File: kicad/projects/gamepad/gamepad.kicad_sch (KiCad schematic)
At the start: 49 parts, among them J1 peripheral_addr_bus_connector, J2 peripheral_aux_connector, J3 peripheral_membank_connector, J4 Conn_01x02_Socket, J5 Conn_01x02_Socket, J6 Conn_02x05_Odd_Even, U1 74HC161, U10 74HC245, U11 74HC245, U12 74HC245, U13 74HC245, U2 74HC161, U3 74HC595, U4 74HC595, U5 74HC595, U6 74HC595, U7 74HC14, U8 74HC08, U9 74HC109

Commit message: Start work on gamepad schematic.
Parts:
- added C10, C11, C12, C13: C, Capacitor_THT:C_Disc_D5.0mm_W2.5mm_P5.00mm, symbol Device:C
- added J7, J8: Conn_01x05_Socket, symbol Connector:Conn_01x05_Socket
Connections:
- net DATA_BUS_00: now also U13.9 (A8)
- net DATA_BUS_01: now also U13.8 (A7)
- net DATA_BUS_02: now also U13.7 (A6)
- net DATA_BUS_03: now also U13.6 (A5)
- net DATA_BUS_04: now also U13.5 (A3)
- net DATA_BUS_05: now also U13.4 (A3)
- net DATA_BUS_06: now also U13.3 (A2)
- net DATA_BUS_07: now also U13.2 (A1)
- net DATA_BUS_08: now also U12.9 (A8)
- net DATA_BUS_09: now also U12.8 (A7)
- net DATA_BUS_10: now also U12.7 (A6)
- net DATA_BUS_11: now also U12.6 (A5)
- net DATA_BUS_12: now also U12.5 (A3)
- net DATA_BUS_13: now also U12.4 (A3)
- net DATA_BUS_14: now also U12.3 (A2)
- net DATA_BUS_15: now also U12.2 (A1)
- net GND: now also C1.2, C2.2, C3.2, C4.2, U1.8 (GND), U12.1 (DIR), U12.10 (GND), U13.1 (DIR), U13.10 (GND), U2.3 (P0), U2.4 (P1), U2.5 (P2), U2.6 (P3), U2.8 (GND), U3.13 (~{OE}), U3.8 (GND), U4.13 (~{OE}), U4.8 (GND), U9.3 (~{K}), C12.2, C13.2
- net VCC: now also C1.1, C2.1, C3.1, C4.1, U1.1 (~{MR}), U1.10 (TE), U1.16 (VCC), U1.7 (PE), U1.9 (~{SPE}), U12.20 (VCC), U13.20 (VCC), U2.1 (~{MR}), U2.10 (TE), U2.16 (VCC), U2.7 (PE), U2.9 (~{SPE}), U3.10 (~{SRCLR}), U3.16 (VCC), U4.10 (~{SRCLR}), U4.16 (VCC), U9.1 (~{CLR}), U9.2 (J), U9.5 (~{PRE}), C12.1, C13.1
- net PAD 1 LED 7: now reaches D8.2 (A)
- net PAD 1 LED 7: now also U10.12 (B7)
- net at U2.15 (TC): now also U8.1
- net SHIFT SERIAL CLK: now reaches U2.2 (CP)
- net SHIFT SERIAL CLK: now also U9.6 (Q)
- net at U11.1 (DIR): now also U11.20 (VCC)
- net PAD 1 ADDR LED: now reaches U11.11 (B8)
- net PAD 1 ADDR LED: now also D13.1 (K)
- net PAD 2 ADDR LED: now reaches U11.12 (B7)
- net PAD 2 ADDR LED: now also D14.1 (K)
- net PAD 1 LED 0: now reaches U11.13 (B6)
- net PAD 1 LED 0: now also D1.2 (A)
- net PAD 1 LED 1: now reaches U11.14 (B5)
- net PAD 1 LED 1: now also D2.2 (A)
- net PAD 1 LED 2: now reaches U11.15 (B4)
- net PAD 1 LED 2: now also D3.2 (A)
- net PAD 1 LED 3: now reaches U11.16 (B3)
- net PAD 1 LED 3: now also D4.2 (A)
- net PAD 1 LED 4: now reaches U11.17 (B2)
- net PAD 1 LED 4: now also D5.2 (A)
- net PAD 1 LED 5: now reaches U11.18 (B1)
- net PAD 1 LED 5: now also D6.2 (A)
- net PAD 1 SHIFT 07: now reaches U11.2 (A1)
- net PAD 1 SHIFT 07: now also U13.18 (B1), U4.15 (QA)
- net PAD 1 SHIFT 06: now reaches U11.3 (A2)
- net PAD 1 SHIFT 06: now also U13.17 (B2), U4.1 (QB)
- net PAD 1 SHIFT 05: now reaches U11.4 (A3)
- net PAD 1 SHIFT 05: now also U13.16 (B3), U4.2 (QC)
- net PAD 1 SHIFT 04: now reaches U11.5 (A3)
- net PAD 1 SHIFT 04: now also U13.15 (B4), U4.3 (QD)
- net PAD 1 SHIFT 03: now reaches U11.6 (A5)
- net PAD 1 SHIFT 03: now also U13.14 (B5), U4.4 (QE)
- net PAD 1 SHIFT 02: now reaches U11.7 (A6)
- net PAD 1 SHIFT 02: now also U13.13 (B6), U4.5 (QF)
- net PAD 1 SHIFT 01: now reaches U11.8 (A7)
- net PAD 1 SHIFT 01: now also U13.12 (B7), U4.6 (QG)
- net PAD 1 SHIFT 00: now reaches U11.9 (A8)
- net PAD 1 SHIFT 00: now also U13.11 (B8), U4.7 (QH)
- net PAD 1 LED 6: now reaches D7.2 (A)
- net PAD 1 LED 6: now also U10.11 (B8)
- net at U8.10: now also U8.3, U8.5
- net SHIFT OUT REG CLK: now reaches U8.8
- net SHIFT OUT REG CLK: now also C11.1
- net BASE CLK: now reaches U8.9
- net BASE CLK: now also J6.10 (Pin_10), J6.2 (Pin_2), J6.4 (Pin_4), J6.6 (Pin_6), J6.8 (Pin_8), U7.1, U9.4 (C)
- net at J6.1 (Pin_1): now also U1.2 (CP)
- net CLK DIV 2: now reaches J6.3 (Pin_3)
- net CLK DIV 2: now also U1.14 (Q0)
- net CLK DIV 4: now reaches J6.5 (Pin_5)
- net CLK DIV 4: now also U1.13 (Q1)
- net CLK DIV 8: now reaches J6.7 (Pin_7)
- net CLK DIV 8: now also U1.12 (Q2)
- net CLK DIV 16: now reaches J6.9 (Pin_9)
- net CLK DIV 16: now also U1.11 (Q3)
- net PAD 1 LED 11: now reaches D12.2 (A)
- net PAD 1 LED 11: now also U10.16 (B3)
- net at U10.1 (DIR): now also U10.20 (VCC)
- net PAD 1 LED 8: now reaches U10.13 (B6)
- net PAD 1 LED 8: now also D9.2 (A)
- net PAD 1 LED 9: now reaches U10.14 (B5)
- net PAD 1 LED 9: now also D10.2 (A)
- net PAD 1 LED 10: now reaches U10.15 (B4)
- net PAD 1 LED 10: now also D11.2 (A)
- net PAD 1 SHIFT 15: now reaches U10.2 (A1)
- net PAD 1 SHIFT 15: now also U12.18 (B1), U3.15 (QA)
- net PAD 1 SHIFT 14: now reaches U10.3 (A2)
- net PAD 1 SHIFT 14: now also U12.17 (B2), U3.1 (QB)
- net PAD 1 SHIFT 13: now reaches U10.4 (A3)
- net PAD 1 SHIFT 13: now also U12.16 (B3), U3.2 (QC)
- net PAD 1 SHIFT 12: now reaches U10.5 (A3)
- net PAD 1 SHIFT 12: now also U12.15 (B4), U3.3 (QD)
- net PAD 1 SHIFT 11: now reaches U10.6 (A5)
- net PAD 1 SHIFT 11: now also U12.14 (B5), U3.4 (QE)
- net PAD 1 SHIFT 10: now reaches U10.7 (A6)
- net PAD 1 SHIFT 10: now also U12.13 (B6), U3.5 (QF)
- net PAD 1 SHIFT 09: now reaches U10.8 (A7)
- net PAD 1 SHIFT 09: now also U12.12 (B7), U3.6 (QG)
- net PAD 1 SHIFT 08: now reaches U10.9 (A8)
- net PAD 1 SHIFT 08: now also U12.11 (B8), U3.7 (QH)
- net at U7.4: now also U3.14 (SER)
- net ~{BASE CLK}: now reaches U8.4
- net ~{BASE CLK}: now also U7.2
- net GAMEPAD LATCH: now reaches U8.6
- net GAMEPAD LATCH: now also C10.1
- net GAMEPAD CLK: now reaches U9.7 (~{Q})
- net GAMEPAD CLK: now also U8.2
- net ~{PAD 1 OE}: now reaches U13.19 (~{OE})
- net ~{PAD 1 OE}: now also U12.19 (~{OE})
- net at U4.11 (SRCLK): now also U3.11 (SRCLK)
- net at U4.12 (RCLK): now also U3.12 (RCLK)
- net at U4.14 (SER): now also U3.9 (QH')
- no-connect marks 0 -> 8
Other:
- moved on the sheet: C1, C2, C3, C4, D1, D10, D11, D12, D13, D14, D2, D3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

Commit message: Gamepad schematic done.
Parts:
- added C14: C, Capacitor_THT:C_Disc_D5.0mm_W2.5mm_P5.00mm, symbol Device:C
- added J10: Pad 2 SNES, Connector_PinSocket_2.54mm:PinSocket_1x05_P2.54mm_Horizontal, symbol Connector:Conn_01x05_Socket
- added J11: Conn_01x03_Pin, Connector_PinHeader_2.54mm:PinHeader_1x03_P2.54mm_Horizontal, symbol Connector:Conn_01x03_Pin
- added J9: Pad 2 header, Connector_PinSocket_2.54mm:PinSocket_1x05_P2.54mm_Horizontal, symbol Connector:Conn_01x05_Socket
- added R3: 10K, Resistor_THT:R_Axial_DIN0207_L6.3mm_D2.5mm_P10.16mm_Horizontal, symbol Device:R_US
- added TP1: Gamepad Latch, Connector_Pin:Pin_D1.0mm_L10.0mm, symbol Connector:TestPoint
- added TP2: Shift out reg CLK, Connector_Pin:Pin_D1.0mm_L10.0mm, symbol Connector:TestPoint
- added TP3: Shift Serial CLK, Connector_Pin:Pin_D1.0mm_L10.0mm, symbol Connector:TestPoint
- added TP4: Gamepad CLK, Connector_Pin:Pin_D1.0mm_L10.0mm, symbol Connector:TestPoint
- added TP5: Base CLK, Connector_Pin:Pin_D1.0mm_L10.0mm, symbol Connector:TestPoint
- added TP6: ~{Base CLK}, Connector_Pin:Pin_D1.0mm_L10.0mm, symbol Connector:TestPoint
- added TP7: RCO, Connector_Pin:Pin_D1.0mm_L10.0mm, symbol Connector:TestPoint
- added U14: 74HC00, Package_DIP:DIP-14_W7.62mm_Socket, symbol 74xx:74HC00
- J4: value Conn_01x02_Socket -> PAD 1 ACTIVE
- J5: value Conn_01x02_Socket -> PAD 2 ACTIVE
- J7: value Conn_01x05_Socket -> Pad 1 header; footprint (none) -> Connector_PinSocket_2.54mm:PinSocket_1x05_P2.54mm_Horizontal
- J8: value Conn_01x05_Socket -> Pad 1 SNES; footprint (none) -> Connector_PinSocket_2.54mm:PinSocket_1x05_P2.54mm_Horizontal
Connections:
- net BASE CLK: now also TP5.1
- net CTL_CLK: now also J6.1 (Pin_1), U1.2 (CP)
- net DATA_BUS_00: now also U6.7 (QH)
- net DATA_BUS_01: now also U6.6 (QG)
- net DATA_BUS_02: now also U6.5 (QF)
- net DATA_BUS_03: now also U6.4 (QE)
- net DATA_BUS_04: now also U6.3 (QD)
- net DATA_BUS_05: now also U6.2 (QC)
- net DATA_BUS_06: now also U6.1 (QB)
- net DATA_BUS_07: now also U6.15 (QA)
- net DATA_BUS_08: now also U5.7 (QH)
- net DATA_BUS_09: now also U5.6 (QG)
- net DATA_BUS_10: now also U5.5 (QF)
- net DATA_BUS_11: now also U5.4 (QE)
- net DATA_BUS_12: now also U5.3 (QD)
- net DATA_BUS_13: now also U5.2 (QC)
- net DATA_BUS_14: now also U5.1 (QB)
- net DATA_BUS_15: now also U5.15 (QA)
- net GAMEPAD CLK: now also J7.4 (Pin_4), J8.4 (Pin_4), J10.4 (Pin_4), J9.4 (Pin_4), TP4.1
- net GAMEPAD LATCH: now also J7.3 (Pin_3), J8.3 (Pin_3), J10.3 (Pin_3), J9.3 (Pin_3), TP1.1
- net GND: now also C10.2, C11.2, C5.2, C6.2, C7.2, C8.2, C9.2, J7.1 (Pin_1), J8.1 (Pin_1), RN1.1 (common), RN2.1 (common), U10.10 (GND), U11.10 (GND), U5.8 (GND), U6.8 (GND), U7.11, U7.13, U7.7 (GND), U7.9, U8.12, U8.13, U8.7 (GND), U9.12 (C), U9.13 (~{K}), U9.14 (J), U9.8 (GND), C14.2, J10.1 (Pin_1), J11.3 (Pin_3), J9.1 (Pin_1), R3.2, U14.10, U14.12, U14.13, U14.7 (GND), U14.9
- net RFM: now also U14.2, U14.4
- net SHIFT OUT REG CLK: now also U3.12 (RCLK), U4.12 (RCLK), U5.12 (RCLK), U6.12 (RCLK), TP2.1
- net SHIFT SERIAL CLK: now also U3.11 (SRCLK), U4.11 (SRCLK), U5.11 (SRCLK), U6.11 (SRCLK), TP3.1
- net VCC: now also C5.1, C6.1, C7.1, C8.1, C9.1, J7.5 (Pin_5), J8.5 (Pin_5), R1.2, R2.2, U10.1 (DIR), U10.20 (VCC), U11.1 (DIR), U11.20 (VCC), U5.10 (~{SRCLR}), U5.16 (VCC), U6.10 (~{SRCLR}), U6.16 (VCC), U7.14 (VCC), U8.14 (VCC), U9.11 (~{PRE}), U9.15 (~{CLR}), U9.16 (VCC), C14.1, J10.5 (Pin_5), J11.1 (Pin_1), J9.5 (Pin_5), U14.14 (VCC)
- net ~{BASE CLK}: now also TP6.1
- net at D8.1 (K): now also RN1.3 (R2)
- net PAD 2 DATA: now reaches U7.5
- net PAD 2 DATA: now also J10.2 (Pin_2), J9.2 (Pin_2)
- net at U7.6: now also U5.14 (SER)
- net PAD 2 ACTIVE: now reaches J5.1 (Pin_1)
- net PAD 2 ACTIVE: now also J5.2 (Pin_2), U14.1
- net at U2.15 (TC), U8.1: now also TP7.1
- net ~{LED ENABLE}: now reaches U11.19 (~{OE})
- net ~{LED ENABLE}: now also U10.19 (~{OE}), J11.2 (Pin_2), R3.1
- net at D6.1 (K): now also RN2.7 (R6)
- net at D7.1 (K): now also RN1.2 (R1)
- net at D2.1 (K): now also RN2.3 (R2)
- net at D1.1 (K): now also RN2.2 (R1)
- net at D12.1 (K): now also RN1.7 (R6)
- net at D3.1 (K): now also RN2.4 (R3)
- net PAD 1 DATA: now reaches U7.3
- net PAD 1 DATA: now also J7.2 (Pin_2), J8.2 (Pin_2)
- net PAD 1 ACTIVE: now reaches J4.1 (Pin_1)
- net PAD 1 ACTIVE: now also J4.2 (Pin_2), U14.5
- net at D11.1 (K): now also RN1.6 (R5)
- net at R2.1: now also D14.2 (A)
- net at D13.2 (A): now also R1.1
- net PAD 2 ~{OE}: now reaches U5.13 (~{OE})
- net PAD 2 ~{OE}: now also U6.13 (~{OE}), U14.3
- net at U5.9 (QH'): now also U6.14 (SER)
- net at D5.1 (K): now also RN2.6 (R5)
- net at D9.1 (K): now also RN1.4 (R3)
- net at D10.1 (K): now also RN1.5 (R4)
- net at RN2.5 (R4): now also D4.1 (K)
- net ADDR_BUS_00: no longer names the net of J1.17 (A_00)
- net ADDR_BUS_01: no longer names the net of J1.18 (A_01)
- net ADDR_BUS_02: no longer names the net of J1.19 (A_02)
- net ADDR_BUS_03: no longer names the net of J1.20 (A_03)
- net ADDR_BUS_04: no longer names the net of J1.21 (A_04)
- net ADDR_BUS_05: no longer names the net of J1.22 (A_05)
- net ADDR_BUS_06: no longer names the net of J1.23 (A_06)
- net ADDR_BUS_07: no longer names the net of J1.24 (A_07)
- net ADDR_BUS_08: no longer names the net of J1.25 (A_08)
- net ADDR_BUS_09: no longer names the net of J1.26 (A_09)
- net ADDR_BUS_10: no longer names the net of J1.27 (A_10)
- net ADDR_BUS_11: no longer names the net of J1.28 (A_11)
- net ADDR_BUS_12: no longer names the net of J1.29 (A_12)
- net ADDR_BUS_13: no longer names the net of J1.30 (A_13)
- net ADDR_BUS_14: no longer names the net of J1.31 (A_14)
- net ADDR_BUS_15: no longer names the net of J1.32 (A_15)
- net BANK_BUS_00: no longer names the net of J3.1 (B_00)
- net BANK_BUS_01: no longer names the net of J3.2 (B_01)
- net BANK_BUS_02: no longer names the net of J3.3 (B_02)
- net BANK_BUS_03: no longer names the net of J3.4 (B_03)
- net BANK_BUS_04: no longer names the net of J3.5 (B_04)
- net BANK_BUS_05: no longer names the net of J3.6 (B_05)
- net BANK_BUS_06: no longer names the net of J3.7 (B_06)
- net BANK_BUS_07: no longer names the net of J3.8 (B_07)
- net BANK_BUS_08: no longer names the net of J3.9 (B_08)
- net BANK_BUS_09: no longer names the net of J3.10 (B_09)
- net BANK_BUS_10: no longer names the net of J3.11 (B_10)
- net BANK_BUS_11: no longer names the net of J3.12 (B_11)
- net BANK_BUS_12: no longer names the net of J3.13 (B_12)
- net BANK_BUS_13: no longer names the net of J3.14 (B_13)
- net BANK_BUS_14: no longer names the net of J3.15 (B_14)
- net BANK_BUS_15: no longer names the net of J3.16 (B_15)
- net ~{PAD 1 OE} renamed PAD 1 ~{OE}
- net PAD 1 ~{OE}: now also U14.6
- no-connect marks 8 -> 56
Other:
- note added: "Clock divide by 2"
- note added: "Count to 16"
- note added: "Gamepad 1 bus output"
- note added: "Gamepad 1 shifter"
- note added: "Gamepad 1 status and pads addressed LEDs"
- note added: "Gamepad 2 shifter"
- note added: "Gamepad connections"
- note added: "LED enable"
- note added: "Latch and clock timing"
- note added: "Optional input clock divide"
- moved on the sheet: C1, C10, C11, C12, C13, C2, C3, C4, C5, C6, C7, C8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

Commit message: Start routing gamepad PCB.
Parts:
- removed U8: 74HC08, Package_DIP:DIP-14_W7.62mm_Socket, symbol sixteen-bit-computer:74HC08
- removed U9: 74HC109, Package_DIP:DIP-16_W7.62mm_Socket, symbol sixteen-bit-computer:74HC109
- added R4: 10K, Resistor_THT:R_Axial_DIN0207_L6.3mm_D2.5mm_P10.16mm_Horizontal, symbol Device:R_US
- added TP8: Raw Gamepad Latch, Connector_Pin:Pin_D1.0mm_L10.0mm, symbol Connector:TestPoint
- added TP9: Raw Shift out reg CLK, Connector_Pin:Pin_D1.0mm_L10.0mm, symbol Connector:TestPoint
- added U8: 74HC00, Package_DIP:DIP-14_W7.62mm_Socket, symbol 74xx:74HC00
- added U9: 74HC161, Package_DIP:DIP-16_W7.62mm_Socket, symbol sixteen-bit-computer:74HC161
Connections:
- net BASE CLK: now also U14.12, R4.2, U9.2 (CP)
- net GAMEPAD CLK: now also U14.5, U7.8
- net GAMEPAD LATCH: now also U7.12; no longer C10.1
- net GND: now also R4.1, U8.10, U8.12, U8.13, U8.7 (GND), U8.9, U9.3 (P0), U9.4 (P1), U9.5 (P2), U9.6 (P3), U9.8 (GND); no longer U14.10, U14.12, U14.13, U14.9, U7.11, U7.13, U7.9
- net PAD 1 ACTIVE: now also U8.5; no longer U14.5
- net PAD 1 ~{OE}: now also U8.6; no longer U14.6
- net PAD 2 ACTIVE: now also U8.1; no longer U14.1
- net PAD 2 ~{OE}: now also U8.3; no longer U14.3
- net RFM: now also U8.2, U8.4; no longer U14.2, U14.4
- net SHIFT OUT REG CLK: now also U7.10; no longer C11.1
- net SHIFT SERIAL CLK: now also U7.9, U9.14 (Q0)
- net VCC: now also U8.14 (VCC), U9.1 (~{MR}), U9.10 (TE), U9.16 (VCC), U9.7 (PE), U9.9 (~{SPE})
- net ~{BASE CLK}: now also U14.9
- net at TP7.1, U2.15 (TC): now also U14.4
- net at U14.11: now also C11.1, U7.11, TP9.1
- net at U14.8: now also C10.1, U7.13, TP8.1
- new net: U14.1, U14.2, U14.6
- new net: U14.10, U14.13, U14.3
- no-connect marks 56 -> 54
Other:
- note added: "Clock div by 2"
- note removed: "Clock divide by 2"
- moved on the sheet: C1, C10, C11, C12, C13, C14, C2, C3, C4, C5, C6, C7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

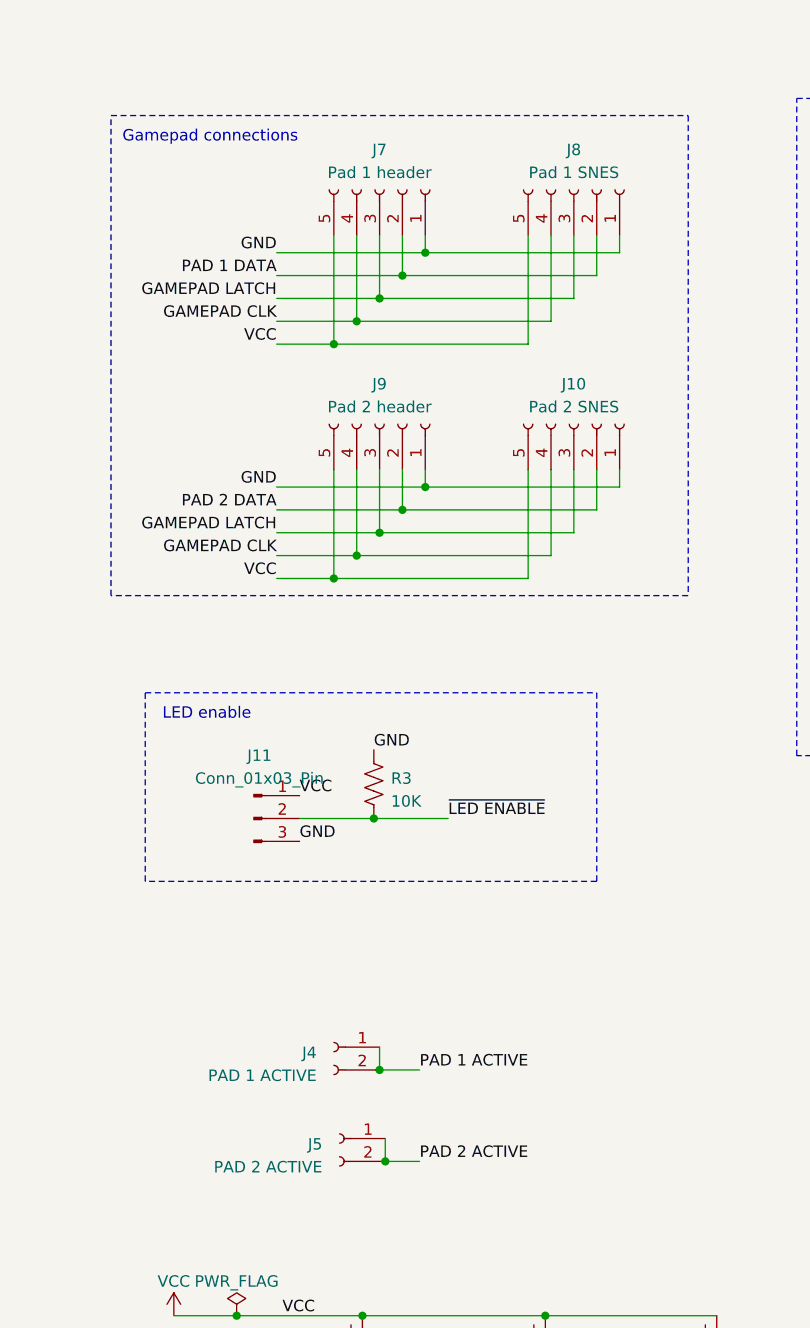
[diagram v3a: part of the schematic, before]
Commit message: Add gamepad connector and almost complete on gamepad PCB
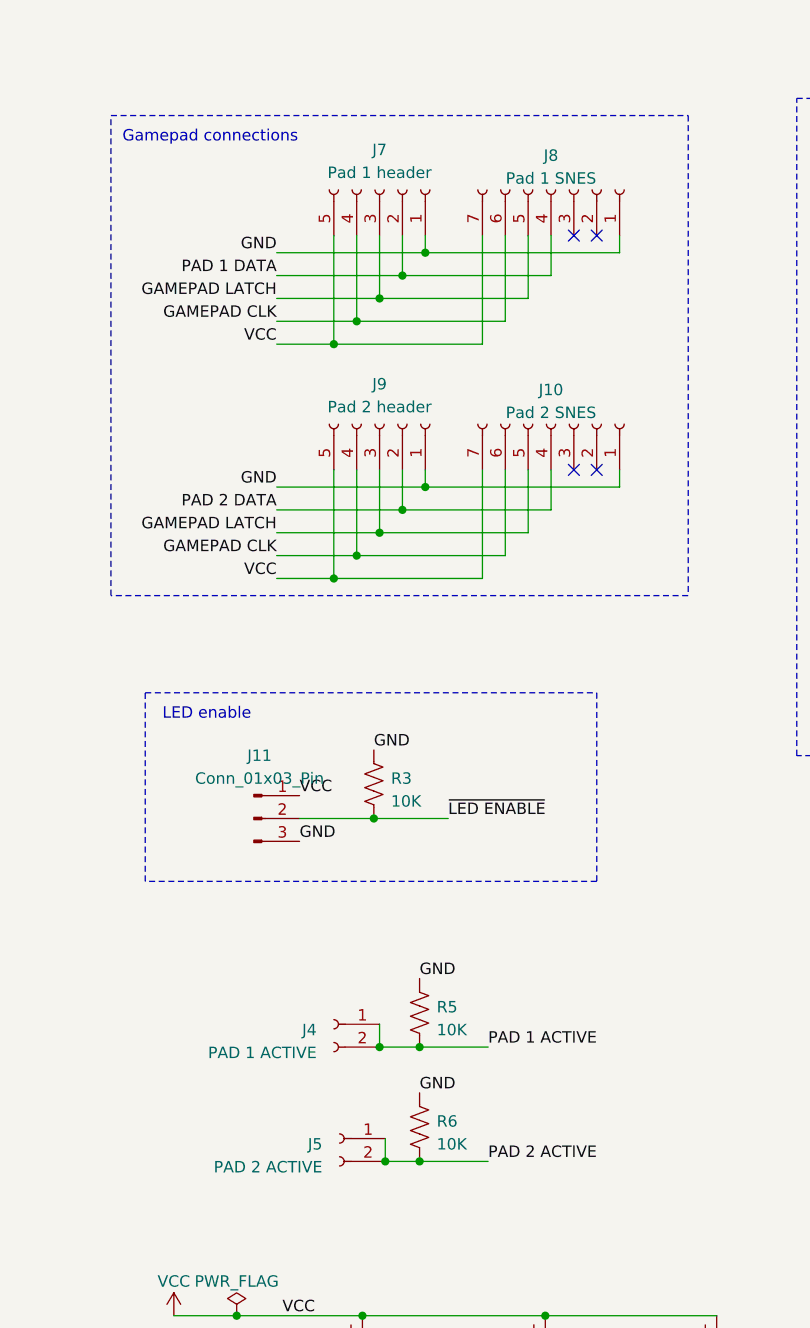
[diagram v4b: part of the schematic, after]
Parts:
- removed J10: Pad 2 SNES, Connector_PinSocket_2.54mm:PinSocket_1x05_P2.54mm_Horizontal, symbol Connector:Conn_01x05_Socket
- removed J8: Pad 1 SNES, Connector_PinSocket_2.54mm:PinSocket_1x05_P2.54mm_Horizontal, symbol Connector:Conn_01x05_Socket
- added J10: Pad 2 SNES, sixteen-bit-computer:snes-rightangle-connector, symbol Connector:Conn_01x07_Socket
- added J8: Pad 1 SNES, sixteen-bit-computer:snes-rightangle-connector, symbol Connector:Conn_01x07_Socket
- added R5, R6: 10K, Resistor_THT:R_Axial_DIN0207_L6.3mm_D2.5mm_P10.16mm_Horizontal, symbol Device:R_US
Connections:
- net GAMEPAD CLK: now also J10.6 (Pin_6), J8.6 (Pin_6)
- net GAMEPAD LATCH: now also J10.5 (Pin_5), J8.5 (Pin_5)
- net GND: now also J10.1 (Pin_1), J8.1 (Pin_1), R5.2, R6.2
- net PAD 1 ACTIVE: now also R5.1
- net PAD 1 DATA: now also J8.4 (Pin_4)
- net PAD 2 ACTIVE: now also R6.1
- net PAD 2 DATA: now also J10.4 (Pin_4)
- net VCC: now also J10.7 (Pin_7), J8.7 (Pin_7)
- no-connect marks 54 -> 58
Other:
- moved on the sheet: J4

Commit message: Gamepad updated to single wie rfm wtm.
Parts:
- added C15, C16: C, Capacitor_THT:C_Disc_D5.0mm_W2.5mm_P5.00mm, symbol Device:C
- C97, C98, C99: value C_Polarized -> 33uF
- R1, R2: value R_US -> 1K
- RN1, RN2: value R_Network08_US -> 2K
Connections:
- net GND: now also C15.1, C16.1; no longer U8.10, U8.12, U8.13, U8.9
- net VCC: now also C15.2, C16.2
- net MEMACTIVE_RFM: now reaches U8.11
- net MEMACTIVE_RFM: now also U8.2, U8.4
- net at U8.8: now also U8.12
- removed net RFM: J2.10 (RFM), U8.2, U8.4
- net WTM renamed RFM_WTM
- net RFM_WTM: now also U8.10, U8.9
- new net MEM_ACTIVE: J2.10 (MEM_ACT), U8.13
- no-connect marks 58 -> 56
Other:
- moved on the sheet: J2, U8D

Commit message: Gamepad updates. Fix memactive RFM. Fix miswired Pad 1 data and pas 1 and 2 read LEDs.
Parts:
- added C17: C, Capacitor_THT:C_Disc_D5.0mm_W2.5mm_P5.00mm, symbol Device:C
- added U15: 74HC00, Package_DIP:DIP-14_W7.62mm_Socket, symbol 74xx:74HC00
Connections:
- net GND: now also U8.10, U8.12, U8.13, U8.9, C17.2, U15.12, U15.13, U15.7 (GND)
- net MEMACTIVE_RFM: now also U15.8; no longer U8.11
- net MEM_ACTIVE: now also U15.5; no longer U8.13
- net PAD 1 ADDR LED: now also D14.1 (K), U10.16 (B3); no longer D13.1 (K), U11.11 (B8)
- net PAD 1 LED 0: now also U11.11 (B8); no longer U11.13 (B6)
- net PAD 1 LED 1: now also U11.12 (B7); no longer U11.14 (B5)
- net PAD 1 LED 10: now also U10.13 (B6); no longer U10.15 (B4)
- net PAD 1 LED 11: now also U10.14 (B5); no longer U10.16 (B3)
- net PAD 1 LED 2: now also U11.13 (B6); no longer U11.15 (B4)
- net PAD 1 LED 3: now also U11.14 (B5); no longer U11.16 (B3)
- net PAD 1 LED 4: now also U11.15 (B4); no longer U11.17 (B2)
- net PAD 1 LED 5: now also U11.16 (B3); no longer U11.18 (B1)
- net PAD 1 LED 6: now also U11.17 (B2); no longer U10.11 (B8)
- net PAD 1 LED 7: now also U11.18 (B1); no longer U10.12 (B7)
- net PAD 1 LED 8: now also U10.11 (B8); no longer U10.13 (B6)
- net PAD 1 LED 9: now also U10.12 (B7); no longer U10.14 (B5)
- net PAD 1 SHIFT 12: no longer U10.5 (A3)
- net PAD 1 SHIFT 13: no longer U10.4 (A3)
- net PAD 1 SHIFT 14: no longer U10.3 (A2)
- net PAD 1 SHIFT 15: no longer U10.2 (A1)
- net PAD 1 ~{OE}: now also U10.4 (A3)
- net PAD 2 ADDR LED: now also D13.1 (K), U10.15 (B4); no longer D14.1 (K), U11.12 (B7)
- net PAD 2 ~{OE}: now also U10.5 (A3)
- net RFM_WTM: now also U15.1, U15.2; no longer U8.10, U8.9
- net VCC: now also C17.1, U15.14 (VCC)
- net at D8.1 (K): now also RN2.9 (R8); no longer RN1.3 (R2)
- net at D7.1 (K): now also RN2.8 (R7); no longer RN1.2 (R1)
- net at U8.8: no longer U8.12
- net at D12.1 (K): now also RN1.5 (R4); no longer RN1.7 (R6)
- net at U10.17 (B2): now also RN1.6 (R5)
- net at U10.18 (B1): now also RN1.7 (R6)
- net at D11.1 (K): now also RN1.4 (R3); no longer RN1.6 (R5)
- net at D9.1 (K): now also RN1.2 (R1); no longer RN1.4 (R3)
- net at D10.1 (K): now also RN1.3 (R2); no longer RN1.5 (R4)
- net at RN1.8 (R7): now also U10.3 (A2)
- net at RN1.9 (R8): now also U10.2 (A1)
- new net: U15.3, U15.4
- new net: U15.10, U15.6, U15.9
- no-connect marks 56 -> 53
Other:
- moved on the sheet: C15, C16, D1, D10, D11, D12, D13, D14, D2, D3, D4, D5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
